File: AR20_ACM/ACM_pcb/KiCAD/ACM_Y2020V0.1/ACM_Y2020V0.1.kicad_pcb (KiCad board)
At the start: 2 copper layers, 2 parts, among them J1 TC2030-MCP-NL, U1 ATmega328PB-AU

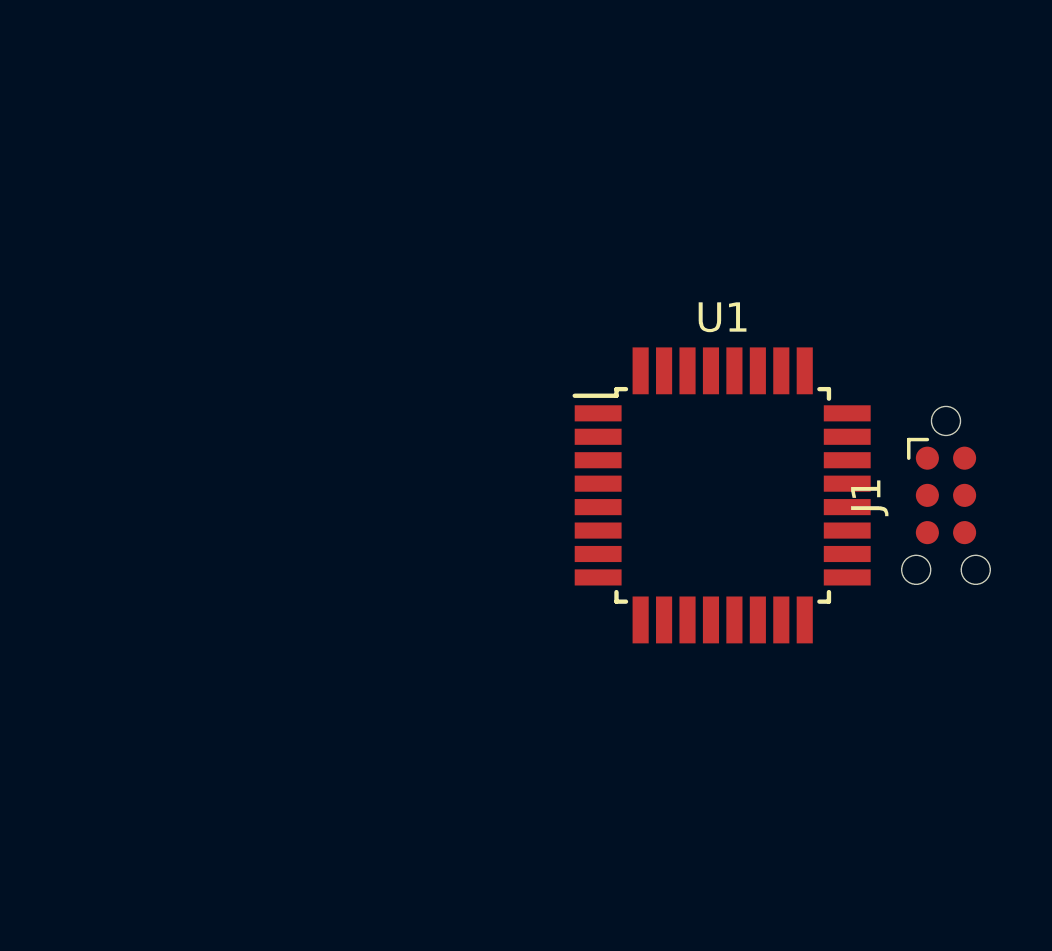
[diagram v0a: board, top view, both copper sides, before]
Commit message: Added MCP25625 and PDFS
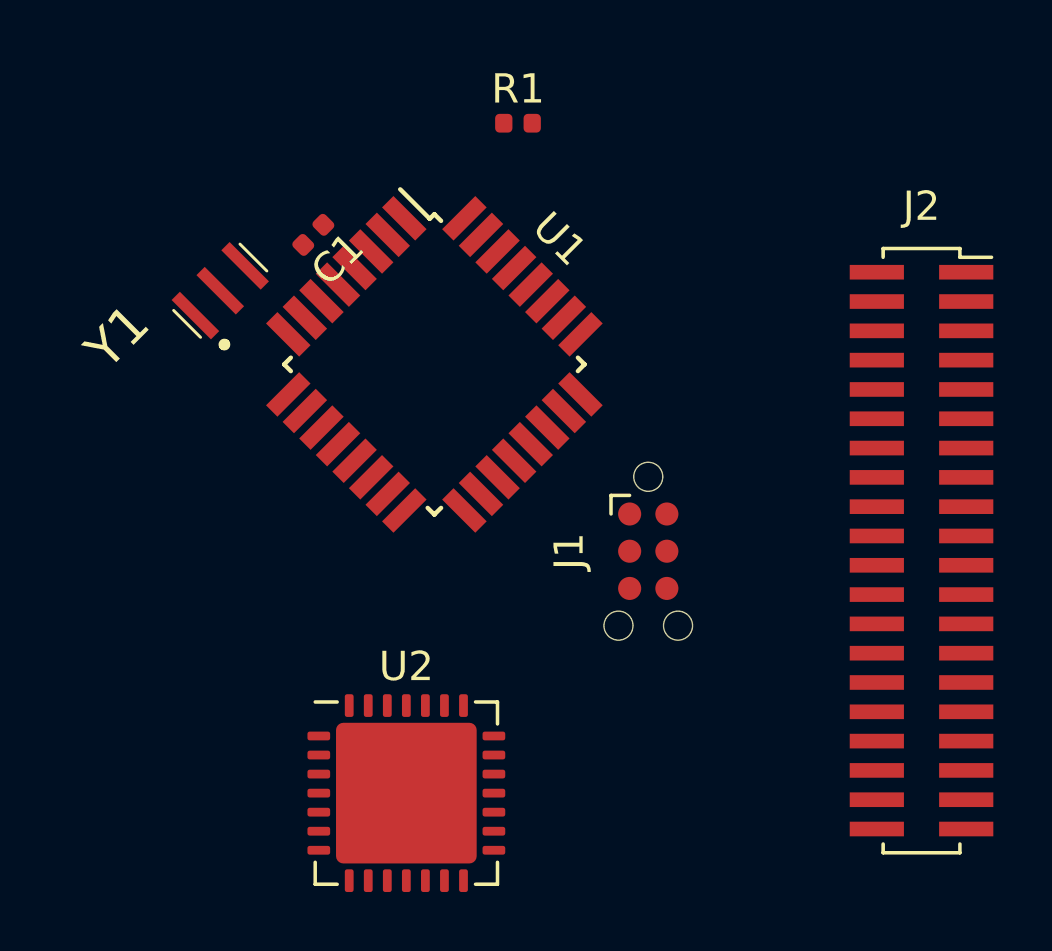
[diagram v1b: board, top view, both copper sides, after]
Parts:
- added C1: 100n, Capacitor_SMD:C_0402_1005Metric, F.Cu at (21.6, 35.6)
- added J2: Conn_02x20_Odd_Even, Connector_PinSocket_1.00mm:PinSocket_2x20_P1.00mm_Vertical_SMD, F.Cu at (42.3, 46.3)
- added R1: 10K, Resistor_SMD:R_0402_1005Metric, F.Cu at (28.6, 31.8)
- added U2: MCP25625-x-SS, Package_DFN_QFN:QFN-28-1EP_6x6mm_P0.65mm_EP4.8x4.8mm, F.Cu at (24.8, 54.6)
- added Y1: 16.0Mhz, CSTNE16M0V530000R0:CSTNE16M0V530000R0, F.Cu at (18.7, 37.8)
- moved U1 10.8 mm to (25.7, 40.0), turned to 315 degrees
- moved J1 10.3 mm to (33.0, 46.4)
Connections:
- net MISO renamed /MISO
- net MOSI renamed /MOSI
- net Reset renamed /Reset
- net SCK renamed /SCK
- J1 pad 5: 5V -> +5V
- U1 pad 18: Net-(U1-Pad18) -> +5V
- U1 pad 20: Net-(U1-Pad20) -> +5V
- U1 pad 21: Net-(U1-Pad21) -> GND
- U1 pad 4: Net-(U1-Pad4) -> +5V
- U1 pad 5: Net-(U1-Pad21) -> GND

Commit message: See change log for update.
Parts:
- added C2: 0.1uF, Capacitor_SMD:C_0402_1005Metric, F.Cu at (25.4, 68.6)
- added C3: 0.1uF, Capacitor_SMD:C_0402_1005Metric, F.Cu at (29.8, 61.6)
- added C4: 0.1uF, Capacitor_SMD:C_0402_1005Metric, F.Cu at (29.8, 66.7)
- added C5: 0.1uF, Capacitor_SMD:C_0402_1005Metric, F.Cu at (35.9, 63.4)
- added D1: 15V, Diode_SMD:D_SOD-323F, F.Cu at (38.0, 16.2)
- added F1: 200mA, Fuse:Fuse_0603_1608Metric, F.Cu at (38.0, 18.0)
- added R2: 120Ohm, Resistor_SMD:R_0603_1608Metric, F.Cu at (15.2, 54.6)
- added R3: 10KOhm, Resistor_SMD:R_0402_1005Metric, F.Cu at (38.8, 63.4)
- added U3: SPX3819M5-L-5-0, Package_TO_SOT_SMD:SOT-23-5, F.Cu at (41.5, 19.0)
- moved J2 36.9 mm to (22.9, 15.0), turned to 90 degrees
- moved R1 26.5 mm to (45.0, 52.5)
- moved U2 14.8 mm to (22.5, 40.0), turned to 135 degrees
- moved J1 14.4 mm to (32.5, 32.0), turned to 45 degrees
- moved C1 12.7 mm to (19.1, 23.1)
- moved U1 12.7 mm to (23.2, 27.5)
- moved Y1 8.82 mm to (27.5, 38.5), turned to 315 degrees
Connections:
- net Net-(U1-Pad12) renamed /CLK_MCP
- U1 pad 11: Net-(U1-Pad11) -> /CAN_CS
- U1 pad 32: Net-(U1-Pad32) -> /CAN_INT
- U2 pad 1: Net-(U2-Pad1) -> Net-(C2-Pad1)
- U2 pad 10: Net-(U2-Pad10) -> GND
- U2 pad 13: Net-(U2-Pad13) -> /CAN_INT
- U2 pad 14: Net-(U2-Pad14) -> /SCK
- U2 pad 15: Net-(U2-Pad15) -> /MOSI
- U2 pad 16: Net-(U2-Pad16) -> /MISO
- U2 pad 17: Net-(U2-Pad17) -> /CAN_CS
- U2 pad 19: Net-(U2-Pad19) -> Net-(C2-Pad1)
- U2 pad 24: Net-(U2-Pad24) -> Net-(U2-Pad20)
- U2 pad 26: Net-(U2-Pad26) -> GND
- U2 pad 28: Net-(U2-Pad28) -> Net-(U2-Pad21)
- U2 pad 3: Net-(U2-Pad3) -> /CANL
- U2 pad 4: Net-(U2-Pad4) -> /CANH

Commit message: Changelog for 27.07.2019
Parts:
- added D2: D_Small, Diode_SMD:D_0402_1005Metric, B.Cu at (159.1, 88.8)
- added LED1: SMLP36RGB2W3R, SMLP36RGB2W3R:SMLP36RGB2W3R, F.Cu at (134.7, 92.0)
- added R4: 200 Ohm, Resistor_SMD:R_0402_1005Metric, F.Cu at (134.4, 90.7)
- added R5: 290 Ohm, Resistor_SMD:R_0402_1005Metric, F.Cu at (135.4, 90.7)
- added R6: 190 Ohm, Resistor_SMD:R_0402_1005Metric, F.Cu at (136.4, 90.7)
- D1, F1, U3: moved to B.Cu
- J2: value Conn_02x20_Odd_Even -> Conn_02x15_Odd_Even; footprint Connector_PinSocket_1.00mm:PinSocket_2x20_P1.00mm_Vertical_SMD -> Connector_PinSocket_0.8mm:PinSocket_2x15_P0.08mm_Vertical_SMD; moved to B.Cu
- moved J1 145.8 mm to (166.2, 90.1)
- moved D1 145.3 mm to (163.7, 89.1)
- moved U3 139.2 mm to (164.1, 85.0), turned to 180 degrees
- moved F1 139.0 mm to (158.8, 86.7), turned to 90 degrees
- moved R2 136.2 mm to (143.6, 100.0), turned to 225 degrees
- moved J2 133.0 mm to (139.2, 79.4)
- moved C1 131.2 mm to (136.7, 81.2)
- moved U1 131.0 mm to (140.7, 85.4)
- moved U2 131.0 mm to (140.7, 96.4)
- moved Y1 116.0 mm to (135.1, 81.8), turned to 90 degrees
- moved C2 113.0 mm to (135.1, 95.5)
- moved R3 112.6 mm to (147.0, 94.5)
- moved R1 110.8 mm to (147.0, 95.7)
- moved C3 110.2 mm to (135.1, 94.2)
- moved C4 109.6 mm to (135.2, 97.0)
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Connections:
- net Net-(J2-Pad28) renamed /U-Pin28
- J1 pad 1: GND -> /MISO
- J1 pad 2: /Reset -> +5V
- J1 pad 3: /MOSI -> /SCK
- J1 pad 4: /SCK -> /MOSI
- J1 pad 5: +5V -> /Reset
- J1 pad 6: /MISO -> GND
- J2 pad 1: Net-(J2-Pad1) -> +12V
- J2 pad 10: Net-(J2-Pad10) -> /U-Pin10
- J2 pad 12: Net-(J2-Pad12) -> /U-Pin12
- J2 pad 14: Net-(J2-Pad14) -> /U-Pin14
- J2 pad 16: Net-(J2-Pad16) -> /U-Pin16
- J2 pad 18: Net-(J2-Pad18) -> /U-Pin18
- J2 pad 2: Net-(J2-Pad2) -> GND
- J2 pad 20: Net-(J2-Pad20) -> /U-Pin20
- J2 pad 22: Net-(J2-Pad22) -> /U-Pin22
- J2 pad 24: Net-(J2-Pad24) -> /U-Pin24
- J2 pad 26: Net-(J2-Pad26) -> /U-Pin26
- J2 pad 3: Net-(J2-Pad3) -> +5V
- J2 pad 4: Net-(J2-Pad4) -> GND
- J2 pad 5: Net-(J2-Pad5) -> +5V
- J2 pad 6: Net-(J2-Pad6) -> GND
- J2 pad 8: Net-(J2-Pad8) -> /U-Pin8
- U1 pad 13: Net-(U1-Pad13) -> /RED_LED
- U1 pad 14: Net-(U1-Pad14) -> /BLUE_LED
- U1 pad 19: Net-(U1-Pad19) -> /U-Pin8
- U1 pad 22: Net-(U1-Pad22) -> /U-Pin10
- U1 pad 23: Net-(U1-Pad23) -> /U-Pin12
- U1 pad 24: Net-(U1-Pad24) -> /U-Pin14
- U1 pad 25: Net-(U1-Pad25) -> /U-Pin16
- U1 pad 26: Net-(U1-Pad26) -> /U-Pin18
- U1 pad 27: Net-(U1-Pad27) -> /U-Pin20
- U1 pad 28: Net-(U1-Pad28) -> /U-Pin22
- U1 pad 30: Net-(U1-Pad30) -> /U-Pin24
- U1 pad 31: Net-(U1-Pad31) -> /U-Pin26
- U1 pad 9: Net-(U1-Pad9) -> /GREEN_LED
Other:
- board outline added: 26.5 x 26.6 mm
- rule via_min_size: 0.4 -> 0.2

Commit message: Changelog for 28.07.2019
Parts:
- added Q1: Q_PMOS_DGS, Package_TO_SOT_SMD:SOT-23, B.Cu at (146.7, 86.4)
- added R7: 100K Ohm, Resistor_SMD:R_0402_1005Metric, B.Cu at (148.1, 89.1)
- D1: footprint Diode_SMD:D_SOD-323F -> Diode_SMD:D_SOD-523
- D2: value D_Small -> 2.4V; footprint Diode_SMD:D_0402_1005Metric -> Diode_SMD:D_SOD-523
- F1: value 200mA -> 250mA
- moved J1 24.9 mm to (145.0, 103.2), turned to 0 degrees
- moved U3 18.7 mm to (146.7, 92.0), turned to 270 degrees
- moved D1 18.4 mm to (146.3, 83.4), turned to 90 degrees
- moved R1 14.9 mm to (151.0, 81.4), turned to 225 degrees
- moved D2 12.8 mm to (146.3, 88.9)
- moved F1 11.7 mm to (147.7, 83.2)
- moved R3 9.61 mm to (137.7, 92.1), turned to 135 degrees
- moved C2 8.14 mm to (141.6, 100.4), turned to 225 degrees
- moved C5 7.72 mm to (136.4, 90.8), turned to 135 degrees
- moved LED1 6.23 mm to (134.4, 85.8), turned to 180 degrees
- moved C4 4.23 mm to (138.4, 99.6), turned to 45 degrees
- moved R6 3.83 mm to (133.3, 88.4), turned to 315 degrees
- moved R4 3.46 mm to (134.6, 87.2), turned to 315 degrees
- moved R5 3.20 mm to (134.0, 87.8), turned to 315 degrees
- moved C3 2.45 mm to (137.0, 92.8), turned to 135 degrees
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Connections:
- net /U-Pin28 renamed Net-(J2-Pad28)
- net Net-(J2-Pad13) renamed /U-Pin13
- net Net-(J2-Pad15) renamed /U-Pin15
- net Net-(J2-Pad17) renamed /U-Pin17
- net Net-(J2-Pad19) renamed /U-Pin19
- net Net-(J2-Pad21) renamed /U-Pin21
- net Net-(J2-Pad25) renamed /U-Pin25
- D1 pad 1: +12V -> Net-(D1-Pad1)
- D2 pad 2: GND -> Net-(D2-Pad2)
- F1 pad 1: Net-(D2-Pad1) -> Net-(D1-Pad1)
- J2 pad 11: Net-(J2-Pad11) -> /U-Pin11
- J2 pad 16: /U-Pin16 -> GND
- J2 pad 18: /U-Pin18 -> GND
- J2 pad 2: GND -> /U-Pin2
- J2 pad 23: Net-(J2-Pad23) -> /U-Pin23
- J2 pad 26: /U-Pin26 -> Net-(J2-Pad26)
- J2 pad 27: Net-(J2-Pad27) -> /U-Pin27
- J2 pad 29: Net-(J2-Pad29) -> /U-Pin29
- J2 pad 30: Net-(J2-Pad30) -> /U-Pin30
- J2 pad 4: GND -> /U-Pin4
- J2 pad 5: +5V -> /U-Pin5
- J2 pad 6: GND -> /U-Pin6
- J2 pad 7: Net-(J2-Pad7) -> /U-Pin7
- J2 pad 9: Net-(J2-Pad9) -> /U-Pin9
- R2 pad 1: /CANH -> /U-Pin27
- R2 pad 2: /CANL -> /U-Pin29
- U1 pad 1: Net-(U1-Pad1) -> /U-Pin20
- U1 pad 10: Net-(U1-Pad10) -> /U-Pin23
- U1 pad 19: /U-Pin8 -> /U-Pin11
- U1 pad 2: Net-(U1-Pad2) -> /U-Pin22
- U1 pad 22: /U-Pin10 -> /U-Pin9
- U1 pad 23: /U-Pin12 -> /U-Pin7
- U1 pad 24: /U-Pin14 -> /U-Pin5
- U1 pad 25: /U-Pin16 -> /U-Pin2
- U1 pad 26: /U-Pin18 -> /U-Pin4
- U1 pad 27: /U-Pin20 -> /U-Pin6
- U1 pad 28: /U-Pin22 -> /U-Pin8
- U1 pad 3: Net-(U1-Pad3) -> /U-Pin24
- U1 pad 30: /U-Pin24 -> /U-Pin12
- U1 pad 31: /U-Pin26 -> /U-Pin14
- U1 pad 6: Net-(U1-Pad6) -> /U-Pin30
- U2 pad 3: /CANL -> /U-Pin29
- U2 pad 4: /CANH -> /U-Pin27
- U2 pad 5: Net-(U2-Pad5) -> GND
- U2 pad 9: Net-(U2-Pad9) -> /CLK_MCP
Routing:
- net /CAN_INT: track 0.00 -> 13.3 mm, vias 0 -> 2
- net /U-Pin8: track 0.00 -> 6.46 mm, vias 0 -> 1
- net /U-Pin2: track 0.00 -> 6.03 mm, vias 0 -> 1
- net /U-Pin4: track 0.00 -> 5.56 mm, vias 0 -> 1
- net /U-Pin30: track 0.00 -> 5.35 mm, vias 0 -> 1
- net /U-Pin12: track 0.00 -> 5.34 mm, vias 0 -> 1
- net /U-Pin6: track 0.00 -> 5.10 mm, vias 0 -> 1
- net /U-Pin14: track 0.00 -> 3.87 mm, vias 0 -> 1
- net Net-(D2-Pad1): track 0.00 -> 3.62 mm
- net /U-Pin24: track 0.00 -> 3.37 mm, vias 0 -> 1
- net Net-(D1-Pad1): track 0.00 -> 3.05 mm
- net /U-Pin22: track 0.00 -> 2.74 mm, vias 0 -> 1
- net Net-(D2-Pad2): track 0.00 -> 2.64 mm
- net +12V: track 0.00 -> 2.50 mm
- net /U-Pin20: track 0.00 -> 2.04 mm, vias 0 -> 1
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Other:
- board size 26.5 x 26.6 mm -> 16 x 28.3 mm
- net class Default: clearance 0.2 -> 0.0889; trace_width 0.25 -> 0.0889; via_dia 0.8 -> 0.45; via_drill 0.4 -> 0.2
- rule trace_clearance: 0.2 -> 0.0889
- rule trace_min: 0.2 -> 0.0889
- rule via_min_drill: 0.3 -> 0.2
- rule via_min_size: 0.2 -> 0.45

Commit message: Changelog for 29.07.2019
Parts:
- R2: moved to B.Cu
- moved F1 12.8 mm to (134.9, 83.2)
- moved D1 12.8 mm to (133.4, 83.4)
- moved R1 12.7 mm to (149.1, 93.9), turned to 135 degrees
- moved D2 12.3 mm to (134.0, 88.9)
- moved Q1 12.3 mm to (134.5, 86.5)
- moved R7 12.3 mm to (135.8, 89.2)
- moved U3 12.3 mm to (134.5, 92.0)
- moved J1 12.0 mm to (146.6, 91.3)
- moved R2 4.89 mm to (147.2, 95.7), turned to 0 degrees
- moved Y1 0.89 mm to (134.1, 82.9), turned to 60 degrees
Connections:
- net /U-Pin10 renamed Net-(J2-Pad10)
- net /U-Pin25 renamed Net-(J2-Pad25)
- J2 pad 1: +12V -> /U-Pin1
- J2 pad 27: /U-Pin27 -> +5V
- J2 pad 29: /U-Pin29 -> +12V
- J2 pad 3: +5V -> /U-Pin3
- R2 pad 1: /U-Pin27 -> /U-Pin3
- R2 pad 2: /U-Pin29 -> /U-Pin1
- U2 pad 3: /U-Pin29 -> /U-Pin1
- U2 pad 4: /U-Pin27 -> /U-Pin3
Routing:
- net /CLK_MCP: track 0.00 -> 31.8 mm
- net /U-Pin1: track 0.00 -> 22.6 mm, vias 0 -> 1
- net /U-Pin3: track 0.00 -> 20.8 mm, vias 0 -> 1
- net /Reset: track 0.00 -> 17.4 mm, vias 0 -> 2
- net /MOSI: track 0.00 -> 11.8 mm, vias 0 -> 2
- net /MISO: track 0.00 -> 10.7 mm, vias 0 -> 3
- net /U-Pin11: track 0.00 -> 8.68 mm, vias 0 -> 1
- net /SCK: track 0.00 -> 7.92 mm
- net /U-Pin9: track 0.00 -> 7.38 mm, vias 0 -> 1
- net Net-(U2-Pad21): track 0.00 -> 7.34 mm, vias 0 -> 2
- net /U-Pin7: track 0.00 -> 6.68 mm, vias 0 -> 1
- net Net-(U2-Pad20): track 0.00 -> 6.28 mm
- net /U-Pin5: track 0.00 -> 6.02 mm, vias 0 -> 1
- net Net-(U1-Pad7): track 0.00 -> 3.01 mm
- net Net-(U1-Pad8): track 0.00 -> 2.89 mm
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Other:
- board size 16 x 28.3 mm -> 18.1 x 24.8 mm

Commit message: Changelog for 29.07.2019
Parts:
- added C6: 100nF, Capacitor_SMD:C_0402_1005Metric, F.Cu at (148.8, 87.5)
- added L1: 10uH, Inductor_SMD:L_0603_1608Metric, F.Cu at (148.8, 85.0)
- moved R1 1.89 mm to (147.2, 94.1), turned to 90 degrees
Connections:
- J2 pad 10: Net-(J2-Pad10) -> /Reset
- J2 pad 13: /U-Pin13 -> /SCK
- J2 pad 15: /U-Pin15 -> /MISO
- J2 pad 17: /U-Pin17 -> /MOSI
- J2 pad 19: /U-Pin19 -> /BLUE_LED
- J2 pad 21: /U-Pin21 -> /RED_LED
- J2 pad 25: Net-(J2-Pad25) -> /GREEN_LED
- U1 pad 20: +5V -> Net-(C6-Pad2)
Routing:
- net +5V: track 1.48 -> 63.5 mm, vias 0 -> 6
- net GND: track 1.48 -> 18.4 mm, vias 0 -> 8
- net Net-(C6-Pad2): track 0.00 -> 10.4 mm
- net /MISO: track 10.7 -> 21.0 mm
- net /SCK: track 7.92 -> 18.0 mm, vias 0 -> 1
- net /BLUE_LED: track 0.00 -> 8.95 mm, vias 0 -> 1
- net /RED_LED: track 0.00 -> 8.47 mm, vias 0 -> 1
- net /MOSI: track 11.8 -> 19.8 mm, vias 2 -> 3
- net /GREEN_LED: track 0.00 -> 7.37 mm, vias 0 -> 1
- net /U-Pin23: track 0.00 -> 6.60 mm, vias 0 -> 1
- net /Reset: track 17.4 -> 21.7 mm, vias 2 -> 3
- net Net-(LED1-Pad3): track 0.00 -> 2.46 mm
- net Net-(LED1-Pad2): track 0.00 -> 1.89 mm
- net /U-Pin8: track 6.46 -> 4.74 mm
- net Net-(C2-Pad1): track 1.10 -> 2.47 mm
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- added copper zone on B.Cu, net +5V
- added copper zone on F.Cu, net GND
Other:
- outline, holes or cut-outs redrawn

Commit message: Changelog for 30.07.2019
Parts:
- moved C3 3.24 mm to (137.1, 89.5)
- moved C5 3.24 mm to (136.4, 87.6)
- moved C6 3.24 mm to (148.8, 84.2)
- moved L1 3.24 mm to (148.8, 81.7)
- moved U2 3.24 mm to (140.8, 92.3)
- moved R1 3.24 mm to (147.2, 90.9)
- moved C1 3.24 mm to (136.8, 78.2)
- moved C2 3.24 mm to (141.6, 97.2)
- moved C4 3.24 mm to (138.5, 96.4)
- moved J1 3.24 mm to (146.6, 88.1)
- moved LED1 3.24 mm to (134.5, 82.6)
- moved R3 3.24 mm to (137.8, 88.9)
- moved R4 3.24 mm to (134.6, 84.0)
- moved R5 3.24 mm to (134.0, 84.5)
- moved R6 3.24 mm to (133.4, 85.1)
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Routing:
- net +5V: track 63.5 -> 0.00 mm, vias 6 -> 0
- net /CLK_MCP: track 32.8 -> 0.00 mm
- net /U-Pin1: track 22.6 -> 0.00 mm, vias 1 -> 0
- net /Reset: track 21.7 -> 0.00 mm, vias 3 -> 0
- net /MISO: track 21.0 -> 0.00 mm, vias 3 -> 0
- net /U-Pin3: track 20.5 -> 0.00 mm, vias 1 -> 0
- net /MOSI: track 19.8 -> 0.00 mm, vias 3 -> 0
- net GND: track 18.4 -> 0.00 mm, vias 8 -> 0
- net /SCK: track 18.0 -> 0.00 mm, vias 1 -> 0
- net /CAN_INT: track 13.3 -> 0.00 mm, vias 2 -> 0
- net Net-(C6-Pad2): track 10.4 -> 0.00 mm
- net /BLUE_LED: track 8.95 -> 0.00 mm, vias 1 -> 0
- net /U-Pin11: track 8.72 -> 0.00 mm, vias 1 -> 0
- net /RED_LED: track 8.47 -> 0.00 mm, vias 1 -> 0
- net /U-Pin9: track 7.38 -> 0.00 mm, vias 1 -> 0
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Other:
- board size 18.1 x 24.8 mm -> 18.1 x 23.3 mm
